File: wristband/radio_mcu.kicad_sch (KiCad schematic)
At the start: 10 parts, among them U3 NINA-B111, U4 DWM3000

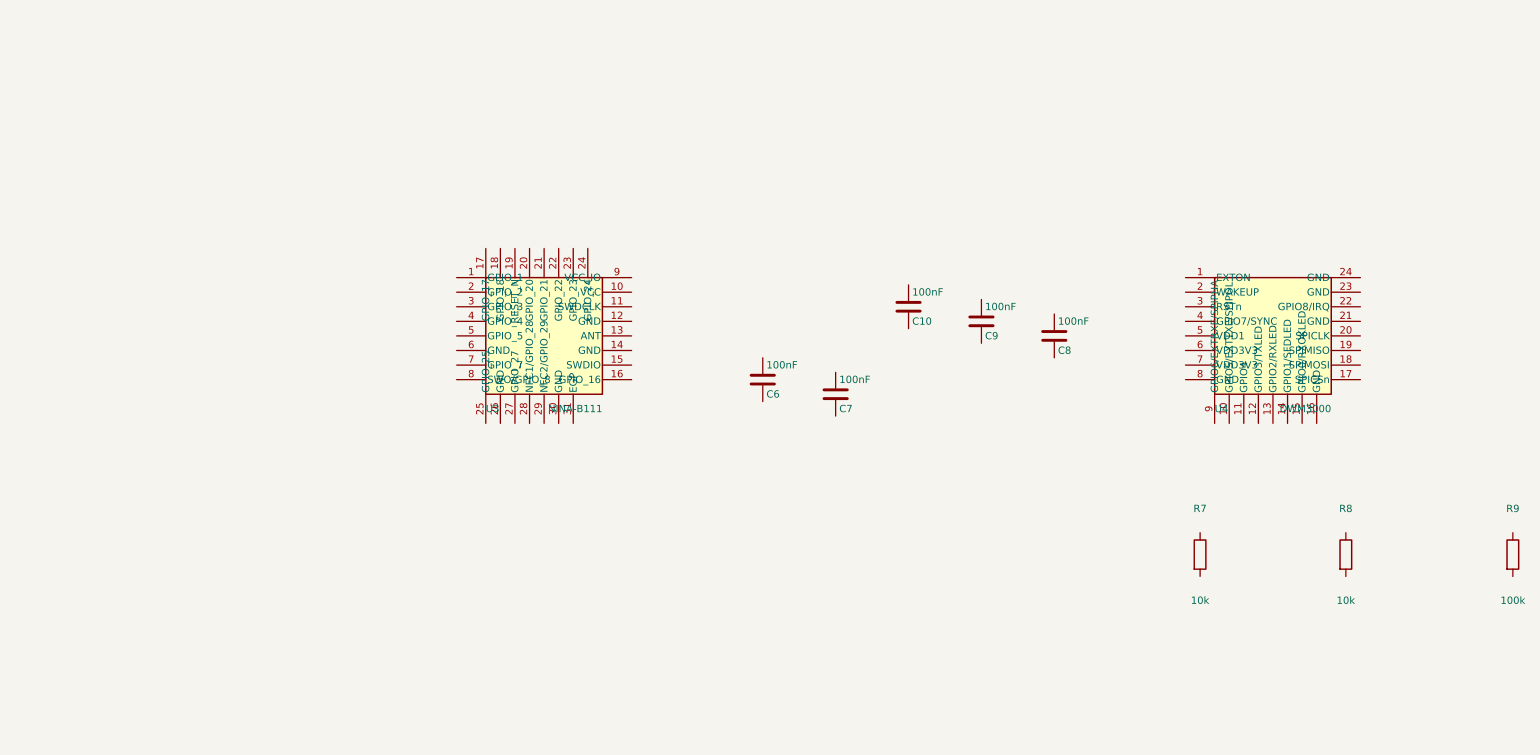
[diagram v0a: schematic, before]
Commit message: Wristband: consolidate onto one DWM3001C, delete the antenna sheet
The tag's BLE radio turned out to serve no purpose -- it talks only over
UWB. Once BLE is not a requirement the question stops being "which BLE
module" and becomes "what is the simplest way to get a Cortex-M4 talking to
a DW3110". That is one DWM3001C: DW3110 transceiver, nRF52833 MCU, LIS2DH12
accelerometer, both antennas, power management and crystal in one part.

Counterintuitively this is the simpler board. A discrete MCU would have
added a second part plus its crystal, decoupling, layout and an inter-chip
SPI bus.

Removed: NINA-B111, DWM3000, antenna.kicad_sch in full (ProAnt InSide-2400,
U.FL connector, L/C matching network), R7/R8 GPIO5/6 straps and R9 IRQ
pulldown -- the host-to-transceiver link is internal now. 8 sheets to 6.
Also closes the "matching-network values pending RF tuning" open item;
there is nothing left to tune.

BLE and the accelerometer are deliberately unused -- dormant silicon on a
module bought for its M4 and its UWB radio. The accelerometer is worth
revisiting to motion-gate the UWB, the largest battery lever available on
the power-constrained side of the system.

Symbol hand-authored, all 48 pins from the real Qorvo DWM3001C Data Sheet
Rev B (May 2022) Table 2, via pdftotext -raw. Caveat carried in the symbol:
pin 18 is not documented in that table, so it is modelled as a passive NC.
Footprint should be imported from a vendor library, not hand-authored --
the land pattern is Figure 5, a drawing.

Side effect: shared/ now contains nothing either board uses. The DWM3000
symbol is kept there deliberately as the fallback until the bay station's
discrete rework is proven.

LDO budget got easier, not harder: 70 mA to 43 mA, headroom 3.6x to 5.8x.
One module doing both jobs draws less than two doing one each.

Also corrects the original DWM3001C rejection in shared/README.md, which
compared it against DWM3000 while holding NINA-B111 fixed -- it never
evaluated replacing both.
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
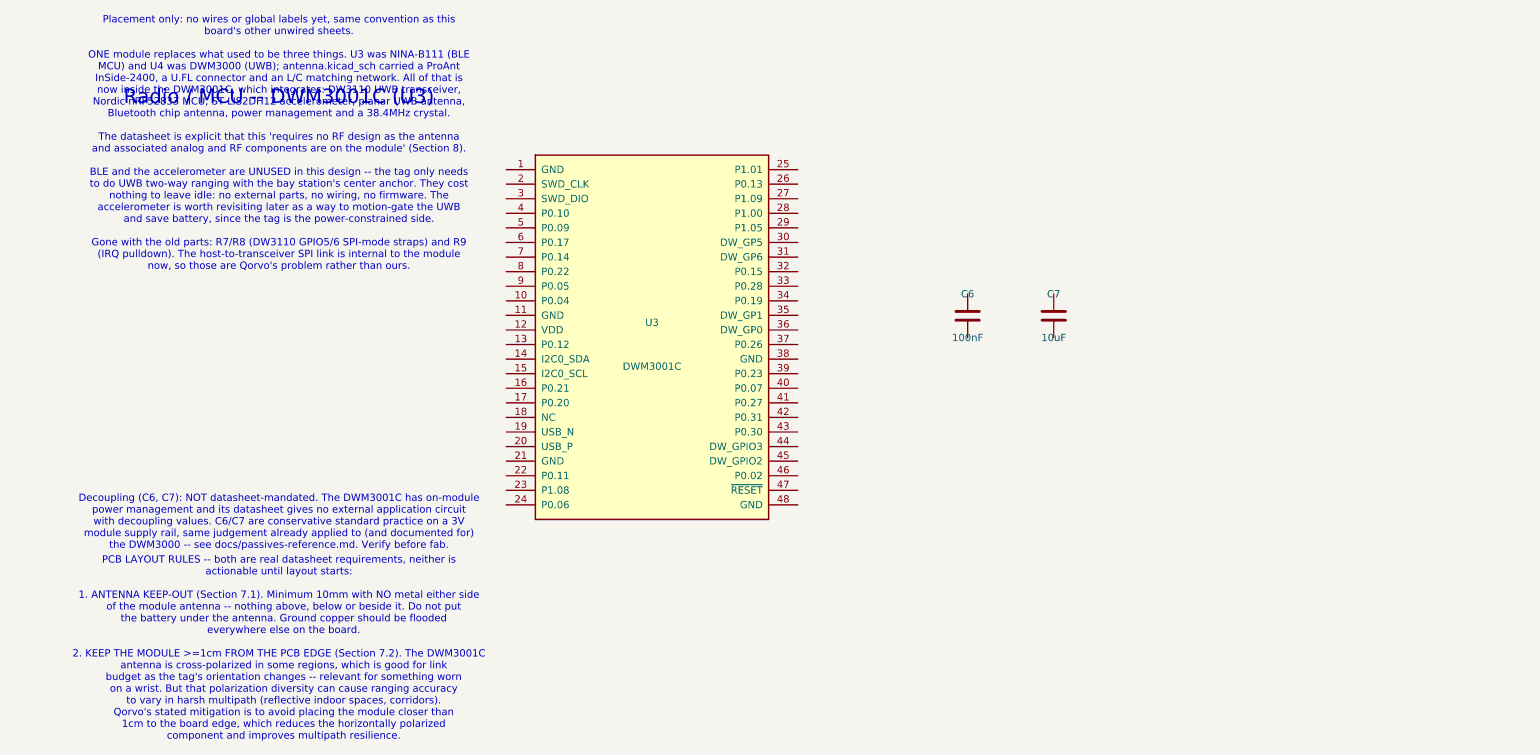
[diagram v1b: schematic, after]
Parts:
- removed C10, C8, C9: 100nF, Capacitor_SMD:C_0603_1608Metric, symbol Device:C
- removed R7, R8: 10k, Resistor_SMD:R_0603_1608Metric, symbol Device:R
- removed R9: 100k, Resistor_SMD:R_0603_1608Metric, symbol Device:R
- removed U3: NINA-B111, wristband:NINA111-42, symbol wristband:NINA-B111
- removed U4: DWM3000, uwb_rescue_locator_shared:DWM3000_PLACEHOLDER, symbol uwb_rescue_locator_shared:DWM3000
- added U3: DWM3001C, symbol wristband:DWM3001C
- C7: value 100nF -> 10uF
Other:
- note added: "Decoupling (C6, C7): NOT datasheet-mandated. The DWM3001C has on-module power management and its datasheet gives no external application circuit with decoupling values. C6/C7 are conservative standard practice on a 3V module supply rail, same judgement already applied to (and documented for) the DWM3000 -- see docs/passives-reference.md. Verify before fab."
- note added: "PCB LAYOUT RULES -- both are real datasheet requirements, neither is actionable until layout starts: 1. ANTENNA KEEP-OUT (Section 7.1). Minimum 10mm with NO metal either side of the module antenna -- nothing above, below or beside it. Do not put the battery under the antenna. Ground copper should be flooded everywhere else on the board. 2. KEEP THE MODULE >=1cm FROM THE PCB EDGE (Section 7.2). Th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"
- note added: "Placement only: no wires or global labels yet, same convention as this board's other unwired sheets. ONE module replaces what used to be three things. U3 was NINA-B111 (BLE MCU) and U4 was DWM3000 (UWB); antenna.kicad_sch carried a ProAnt InSide-2400, a U.FL connector and an L/C matching network. All of that is now inside the DWM3001C, which integrates: DW3110 UWB transceiver, Nordic nRF52833 MCU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"
- note added: "Radio / MCU -- DWM3001C (U3)"
